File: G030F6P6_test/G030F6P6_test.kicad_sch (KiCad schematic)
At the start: 35 parts, among them J1 Conn_01x10_Female, J3 Conn_01x10_Female, J4 USB_C_Receptacle_USB2.0, J5 Conn_01x05_Female, SW1 SW_Push_SPDT, U1 CH343P, U2 STM32G030FxP, U3 XC6206P332MR

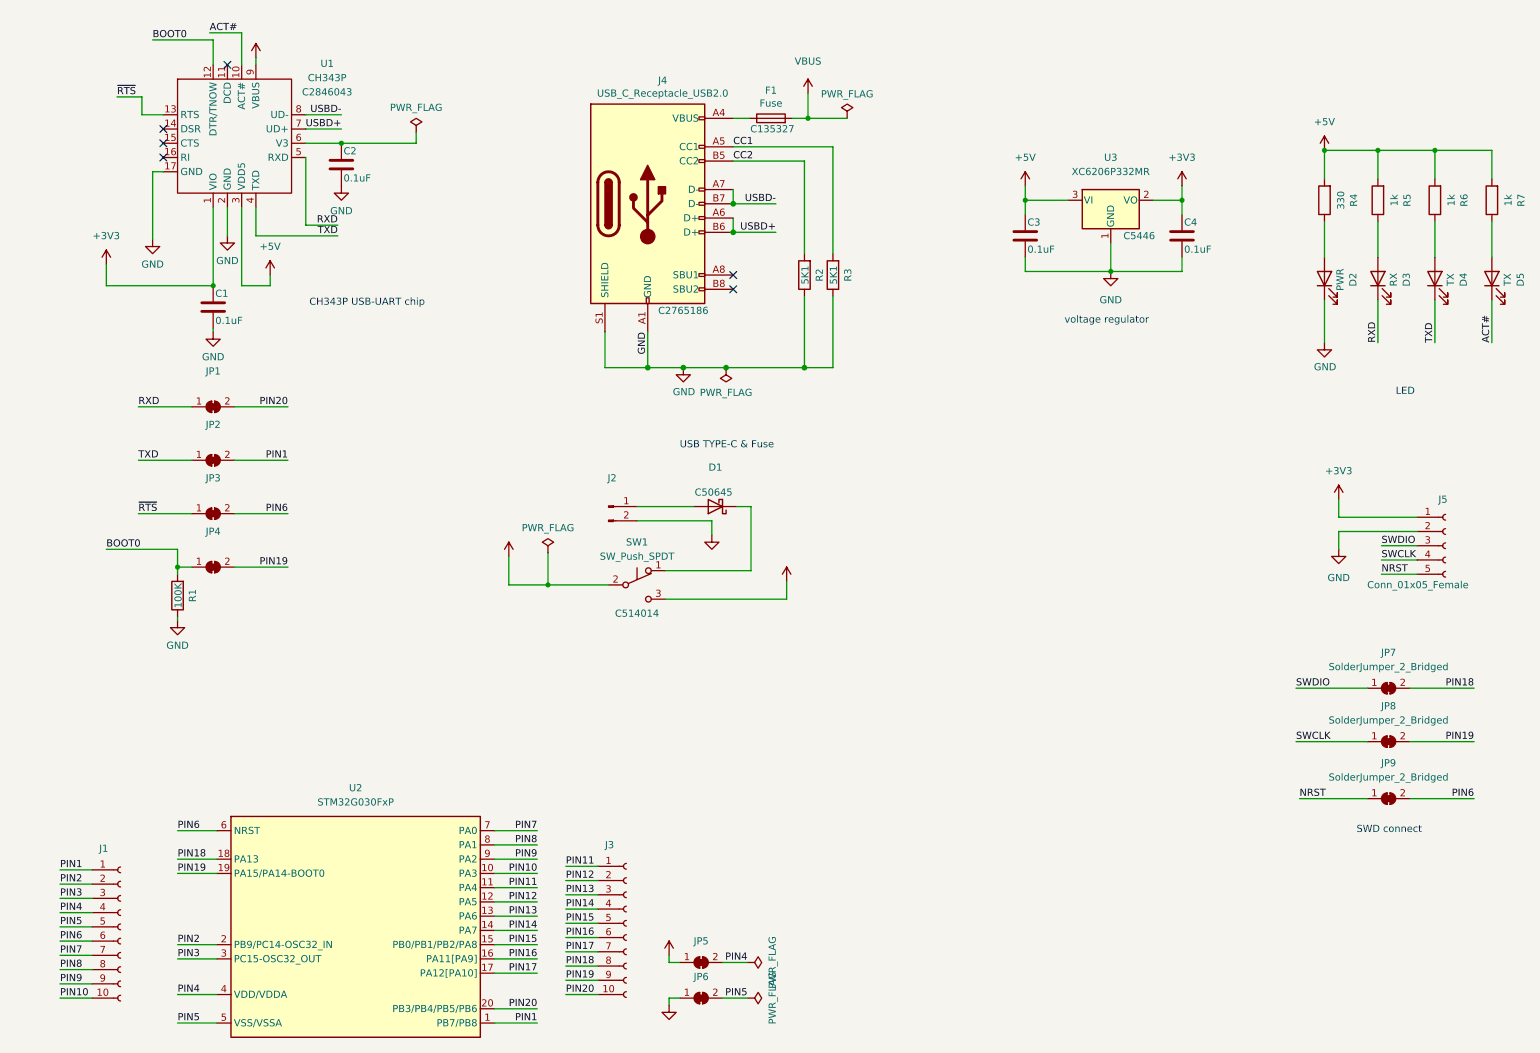
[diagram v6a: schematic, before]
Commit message: Update G030F6P6_test.kicad_sch
fix STM32 電源誤用5V
CH343P 調整位置
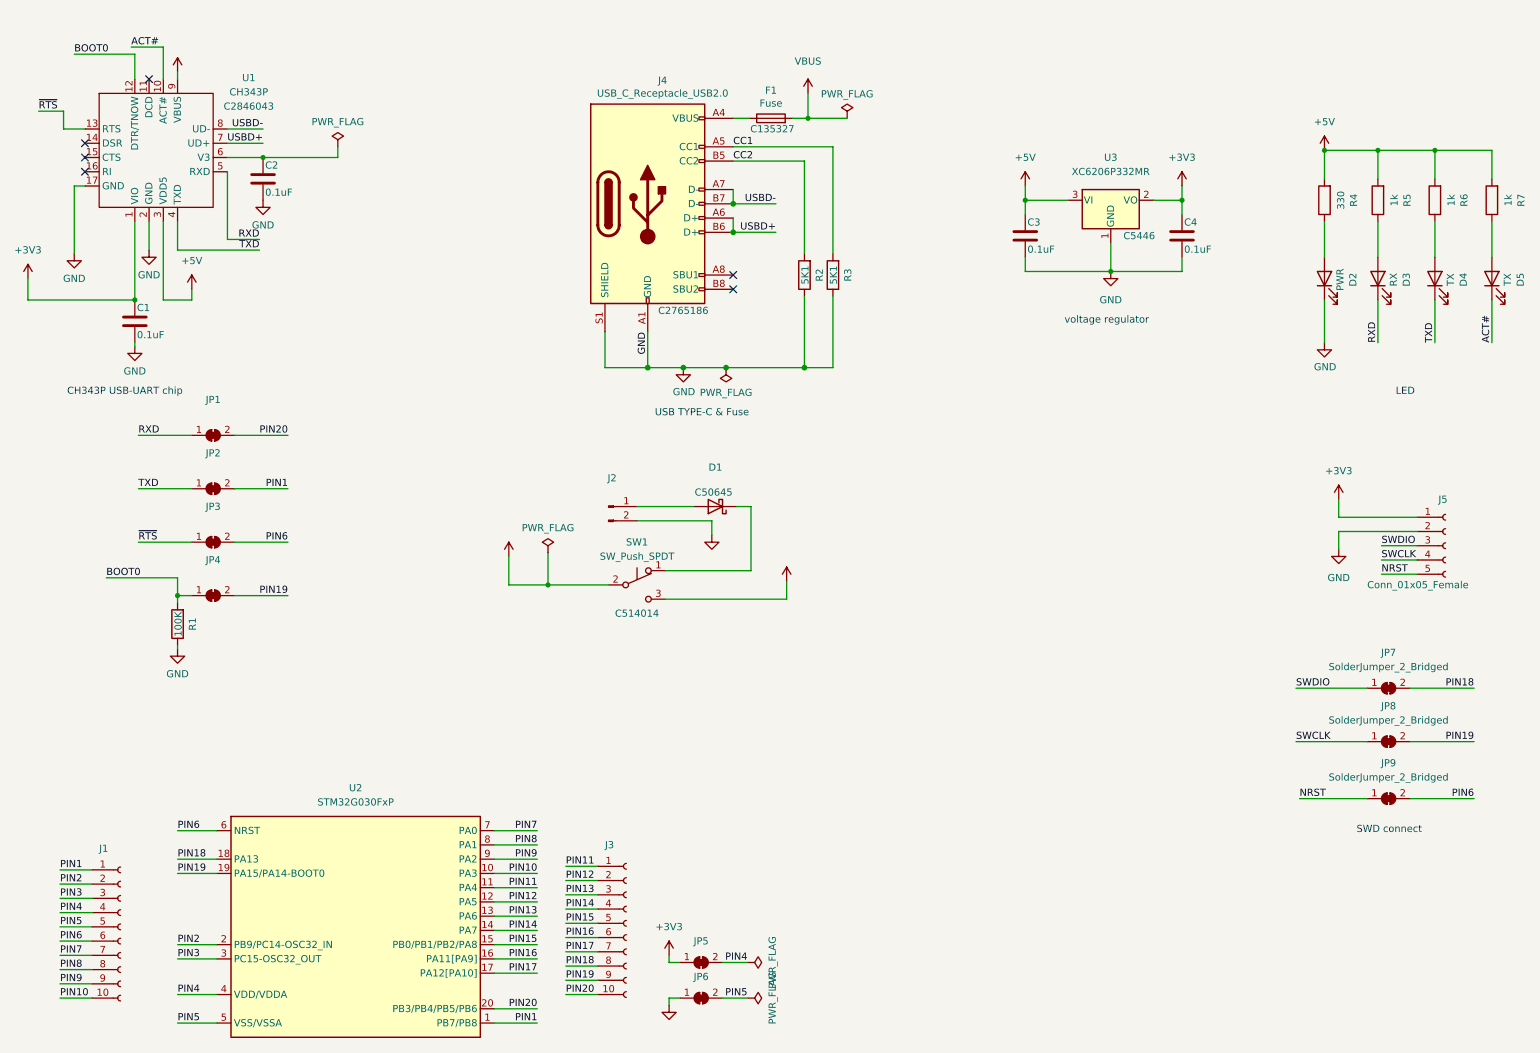
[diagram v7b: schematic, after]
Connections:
- net +3V3: now also JP5.1 (A)
- net +5V: no longer JP5.1 (A)
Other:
- moved on the sheet: C1, C2, JP1, JP2, JP3, JP4, R1, U1

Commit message: Update G030F6P6_test.kicad_sch
更新指示燈名稱
新增CPU 濾波電容
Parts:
- added C?: 0.1uF, Capacitor_SMD:C_0805_2012Metric, symbol Device:C
- D1: value (none) -> D_Schottky; footprint (none) -> Diode_SMD:D_SMA
- D5: value TX -> (none)
- J2: value (none) -> Conn_01x02_Male; footprint (none) -> Connector_PinHeader_2.54mm:PinHeader_1x02_P2.54mm_Horizontal
- JP1, JP2, JP3, JP4, JP5, JP6: value (none) -> SolderJumper_2_Bridged; footprint (none) -> Jumper:SolderJumper-2_P1.3mm_Bridged2Bar_RoundedPad1.0x1.5mm
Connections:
- net PIN4: now also C?.1
- net PIN5: now also C?.2
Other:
- moved on the sheet: JP5
